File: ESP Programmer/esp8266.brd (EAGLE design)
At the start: 22.5 x 38.7 mm, 11 parts

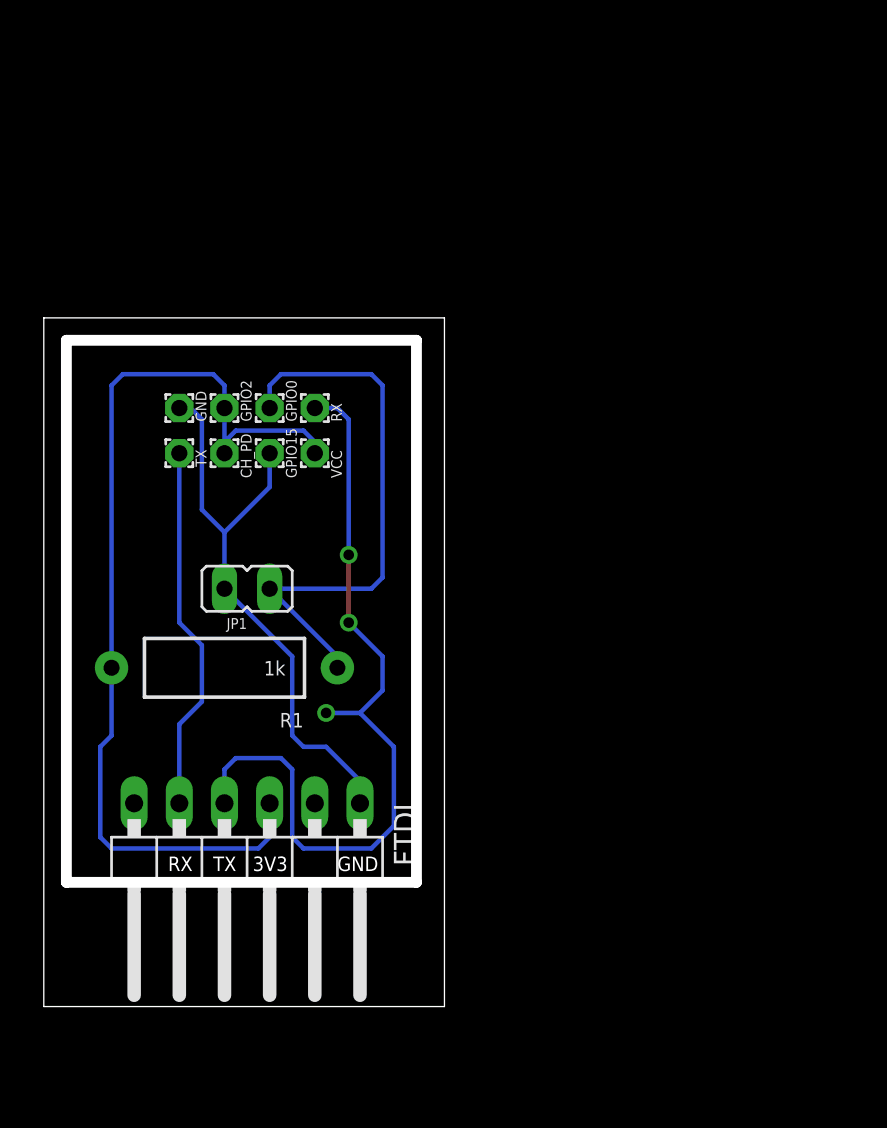
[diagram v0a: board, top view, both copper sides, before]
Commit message: remove old dead projects, add esp-01 sensor stuff
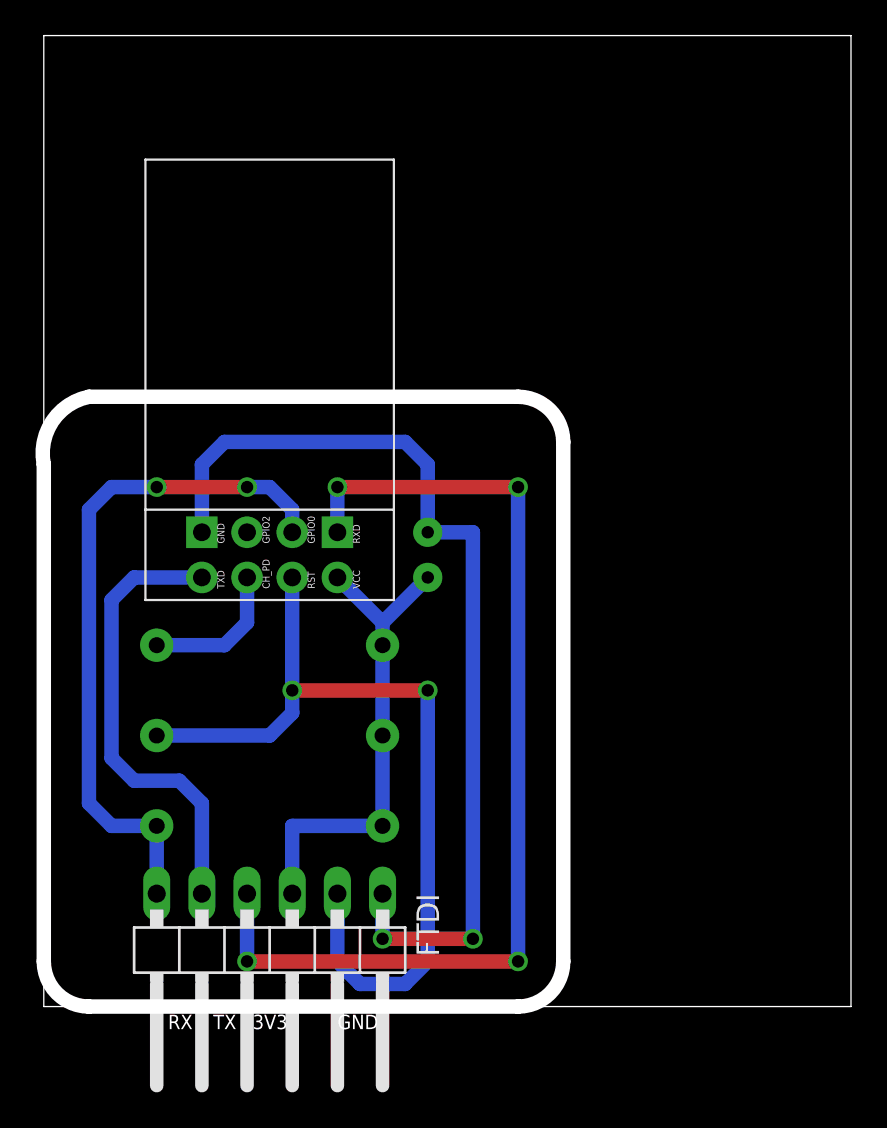
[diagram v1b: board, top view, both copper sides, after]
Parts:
- removed CH_PD, GND, GPIO0, GPIO15, GPIO2, RX, TX, VCC: (no value), wirepad:1,6/0,9
- removed JP1: (no value), jumper:JP1
- added C1: (no value), SparkFun-Capacitors:CAP-PTH-SMALLEZ
- added R2, R3: 10k, SparkFun-Passives:AXIAL-0.5
- added U$1: ESP-01, Franc:ESP-01
- R1: value 1k -> 10k
- moved R1 9.25 mm to (12.7, 10.2), flipped to the bottom, turned to 0 degrees
- moved FTDI 5.24 mm to (12.7, 2.54)
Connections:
- removed net N$1: GPIO0.1, JP1.1, R1.P$1
- new net DTR: FTDI.6, R1.P$2, U$1.GPIO0
- new net N$3: R2.P$1, U$1.CH_PD
- new net RST: FTDI.2, R3.P$1, U$1.RST
- net 3V3: now also C1.1, R1.P$1, R2.P$2, R3.P$2, U$1.VCC; no longer CH_PD.1, GPIO2.1, R1.P$2, VCC.1
- net GND: now also C1.2, U$1.GND; no longer GND.1, GPIO15.1, JP1.2
- net RX: now also U$1.RXD; no longer RX.1
- net TX: now also U$1.TXD; no longer TX.1
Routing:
- net RST: track 0.00 -> 48.6 mm, vias 0 -> 2
- net DTR: track 0.00 -> 38.4 mm, vias 0 -> 2
- net N$1: track 31.6 -> 0.00 mm
- net 3V3: track 54.5 -> 27.5 mm
- net GND: track 33.0 -> 54.4 mm, vias 0 -> 2
- net RX: track 45.6 -> 58.4 mm, vias 3 -> 4
- net N$3: track 0.00 -> 8.15 mm
- net TX: track 20.7 -> 25.7 mm
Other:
- board size 22.5 x 38.7 mm -> 45.4 x 54.6 mm
